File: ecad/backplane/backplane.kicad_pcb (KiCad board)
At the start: 2 copper layers, 220 x 160 mm, 25 parts, among them J1 10145891-0320J13LF, J2 10145891-0320J13LF, J3 10145891-0320J13LF, J4 10145891-0320J13LF, J5 USB4105-GF-A, J6 5017868090, U1 MCP16331x-xCH

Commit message: general team number silkscreen
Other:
- board text added: "ECE 477 Team 15 αCassiopeiae"
- board text added: "rev. 01 3/14/2025"
- board text removed: "ECE 47700: Spring 2025"
- board text removed: "TEAM 15: AlphaCassiopeiae"

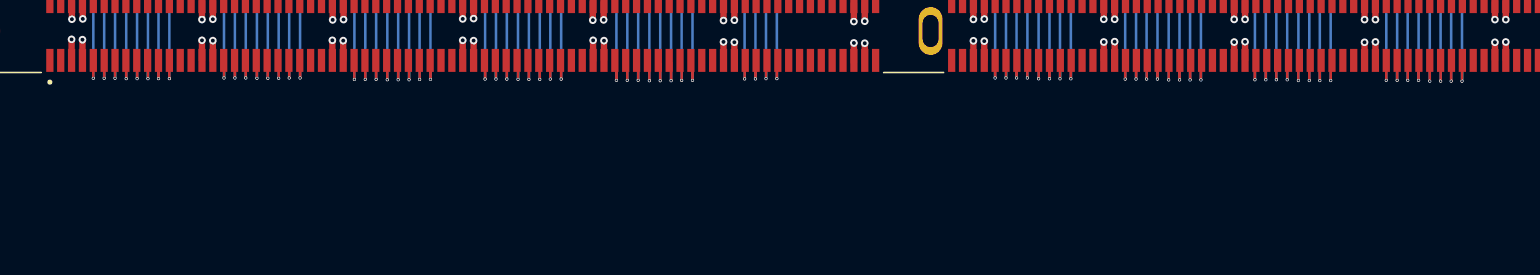
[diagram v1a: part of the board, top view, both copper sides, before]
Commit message: backplane add debug vias
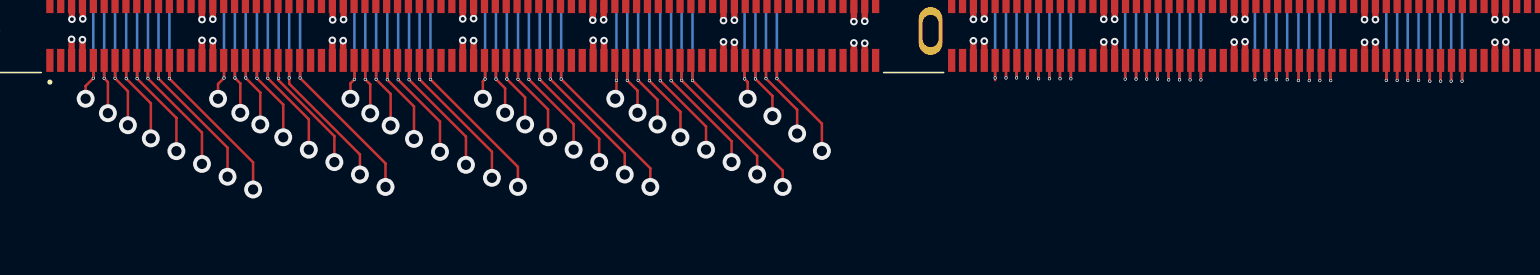
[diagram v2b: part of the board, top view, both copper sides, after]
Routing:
- net CLOCK: track 146.3 -> 157.7 mm, vias 5 -> 6
- net HLDA: track 176.6 -> 187.9 mm, vias 5 -> 6
- net D7: track 156.2 -> 167.5 mm, vias 5 -> 6
- net INP: track 186.9 -> 198.1 mm, vias 5 -> 6
- net A7: track 166.4 -> 177.6 mm, vias 5 -> 6
- net A6: track 165.5 -> 175.6 mm, vias 5 -> 6
- net DBIN: track 145.5 -> 155.4 mm, vias 5 -> 6
- net A11: track 176.3 -> 186.1 mm, vias 5 -> 6
- net D6: track 155.3 -> 165.2 mm, vias 5 -> 6
- net MEMR: track 186.0 -> 195.8 mm, vias 5 -> 6
- net A5: track 164.7 -> 173.2 mm, vias 5 -> 6
- net MWRT: track 144.7 -> 153.1 mm, vias 5 -> 6
- net WAIT: track 174.9 -> 183.3 mm, vias 5 -> 6
- net D5: track 154.5 -> 162.9 mm, vias 5 -> 6
- net M1: track 185.2 -> 193.5 mm, vias 5 -> 6
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
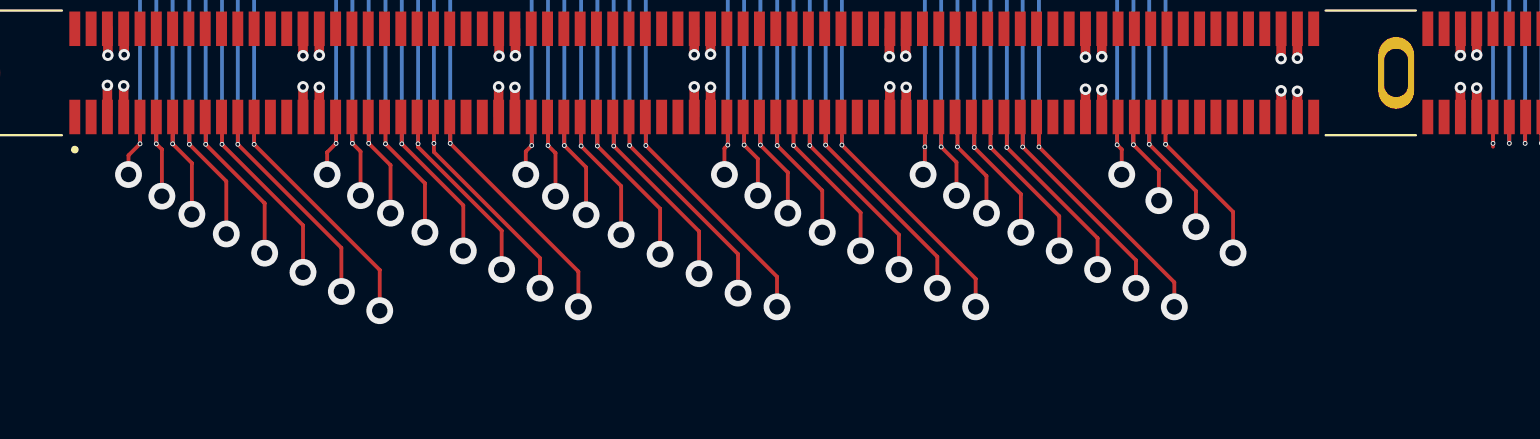
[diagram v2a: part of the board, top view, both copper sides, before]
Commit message: various production cost changes
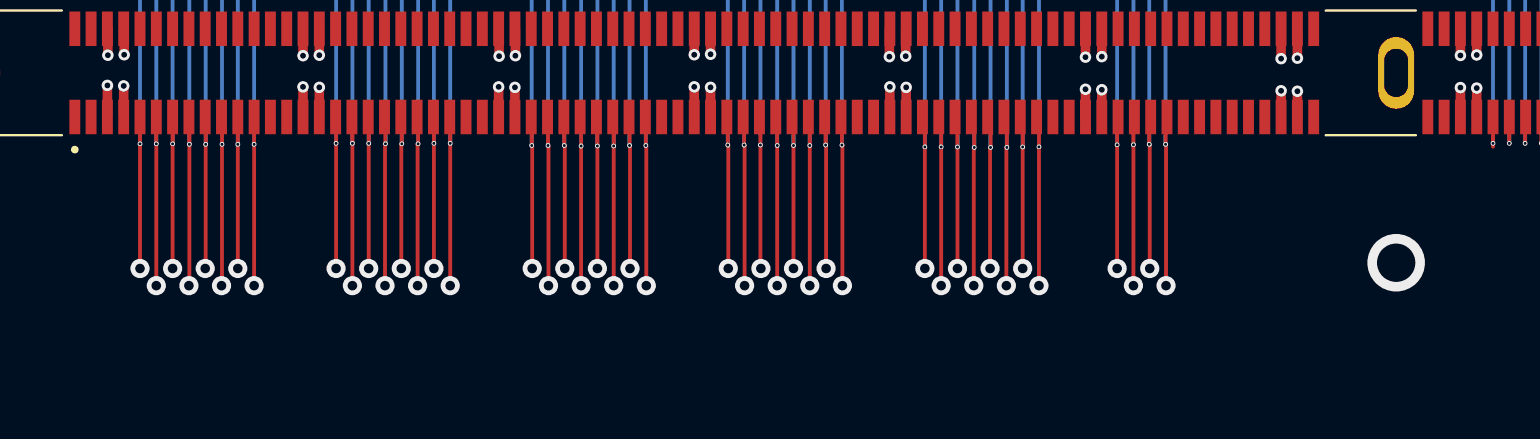
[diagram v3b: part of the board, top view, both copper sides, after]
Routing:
- net A12: track 182.4 -> 187.3 mm
- net A8: track 173.3 -> 178.1 mm
- net HLTA: track 193.0 -> 197.8 mm
- net A0: track 164.8 -> 169.6 mm
- net D0: track 154.7 -> 159.4 mm
- net RESET: track 142.8 -> 147.5 mm
- net PRDY: track 144.7 -> 149.2 mm
- net D1: track 156.7 -> 161.2 mm
- net A1: track 166.8 -> 171.3 mm
- net PROT: track 174.4 -> 178.8 mm
- net A13: track 184.6 -> 189.0 mm
- net INP: track 198.1 -> 194.1 mm
- net CLOCK: track 157.7 -> 153.6 mm
- net HLDA: track 187.9 -> 183.9 mm
- net A7: track 177.6 -> 173.7 mm
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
